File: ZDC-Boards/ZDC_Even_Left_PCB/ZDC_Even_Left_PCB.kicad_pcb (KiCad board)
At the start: 2 copper layers, 202.6 x 643 mm, 102 parts

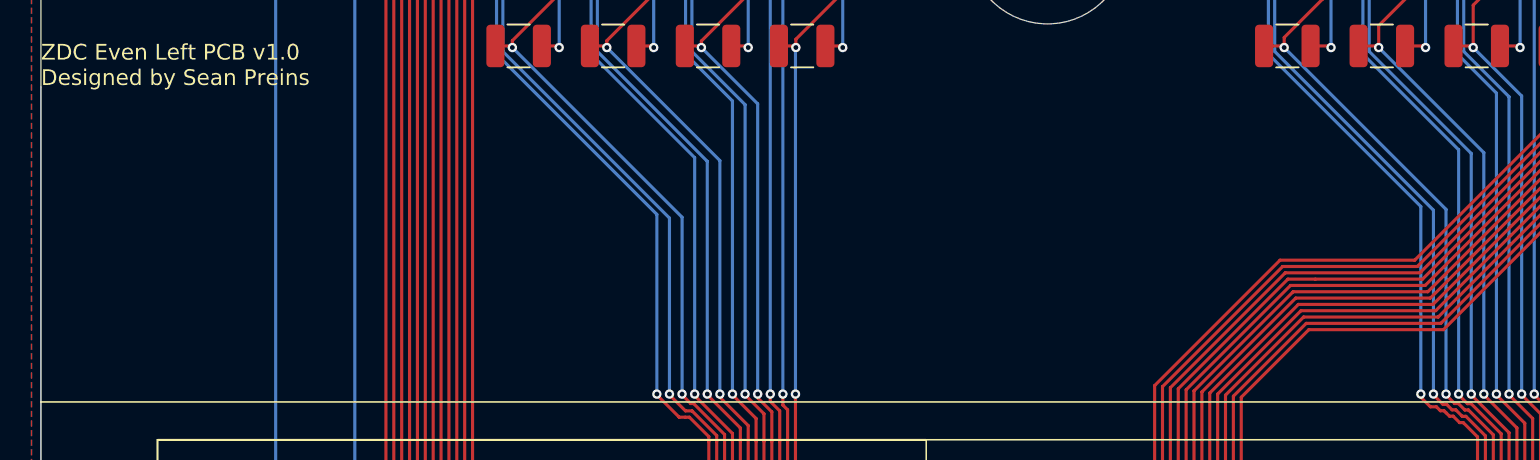
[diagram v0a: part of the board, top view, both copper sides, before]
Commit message: Updated small connector on ZDC PCBs
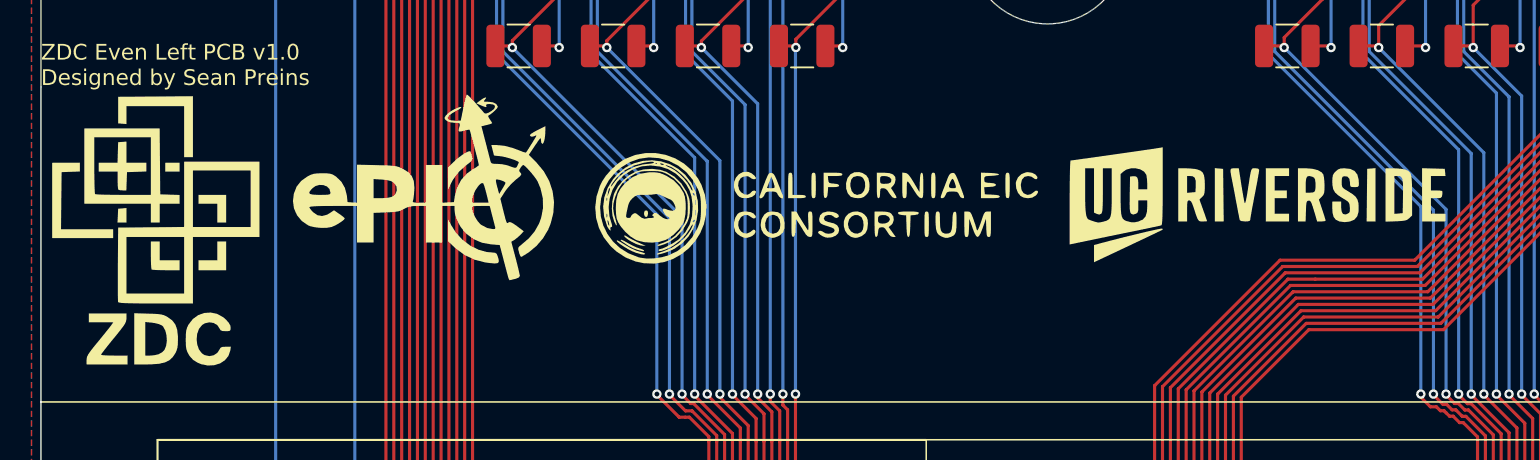
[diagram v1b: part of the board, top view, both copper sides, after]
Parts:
- added G***: LOGO, LOGO, F.Cu at (37.5, -599.0)
